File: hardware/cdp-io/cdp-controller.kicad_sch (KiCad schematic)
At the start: 10 parts, among them U10 74LS175, U7 74LS14, U8 74LS138, U9 74LS138

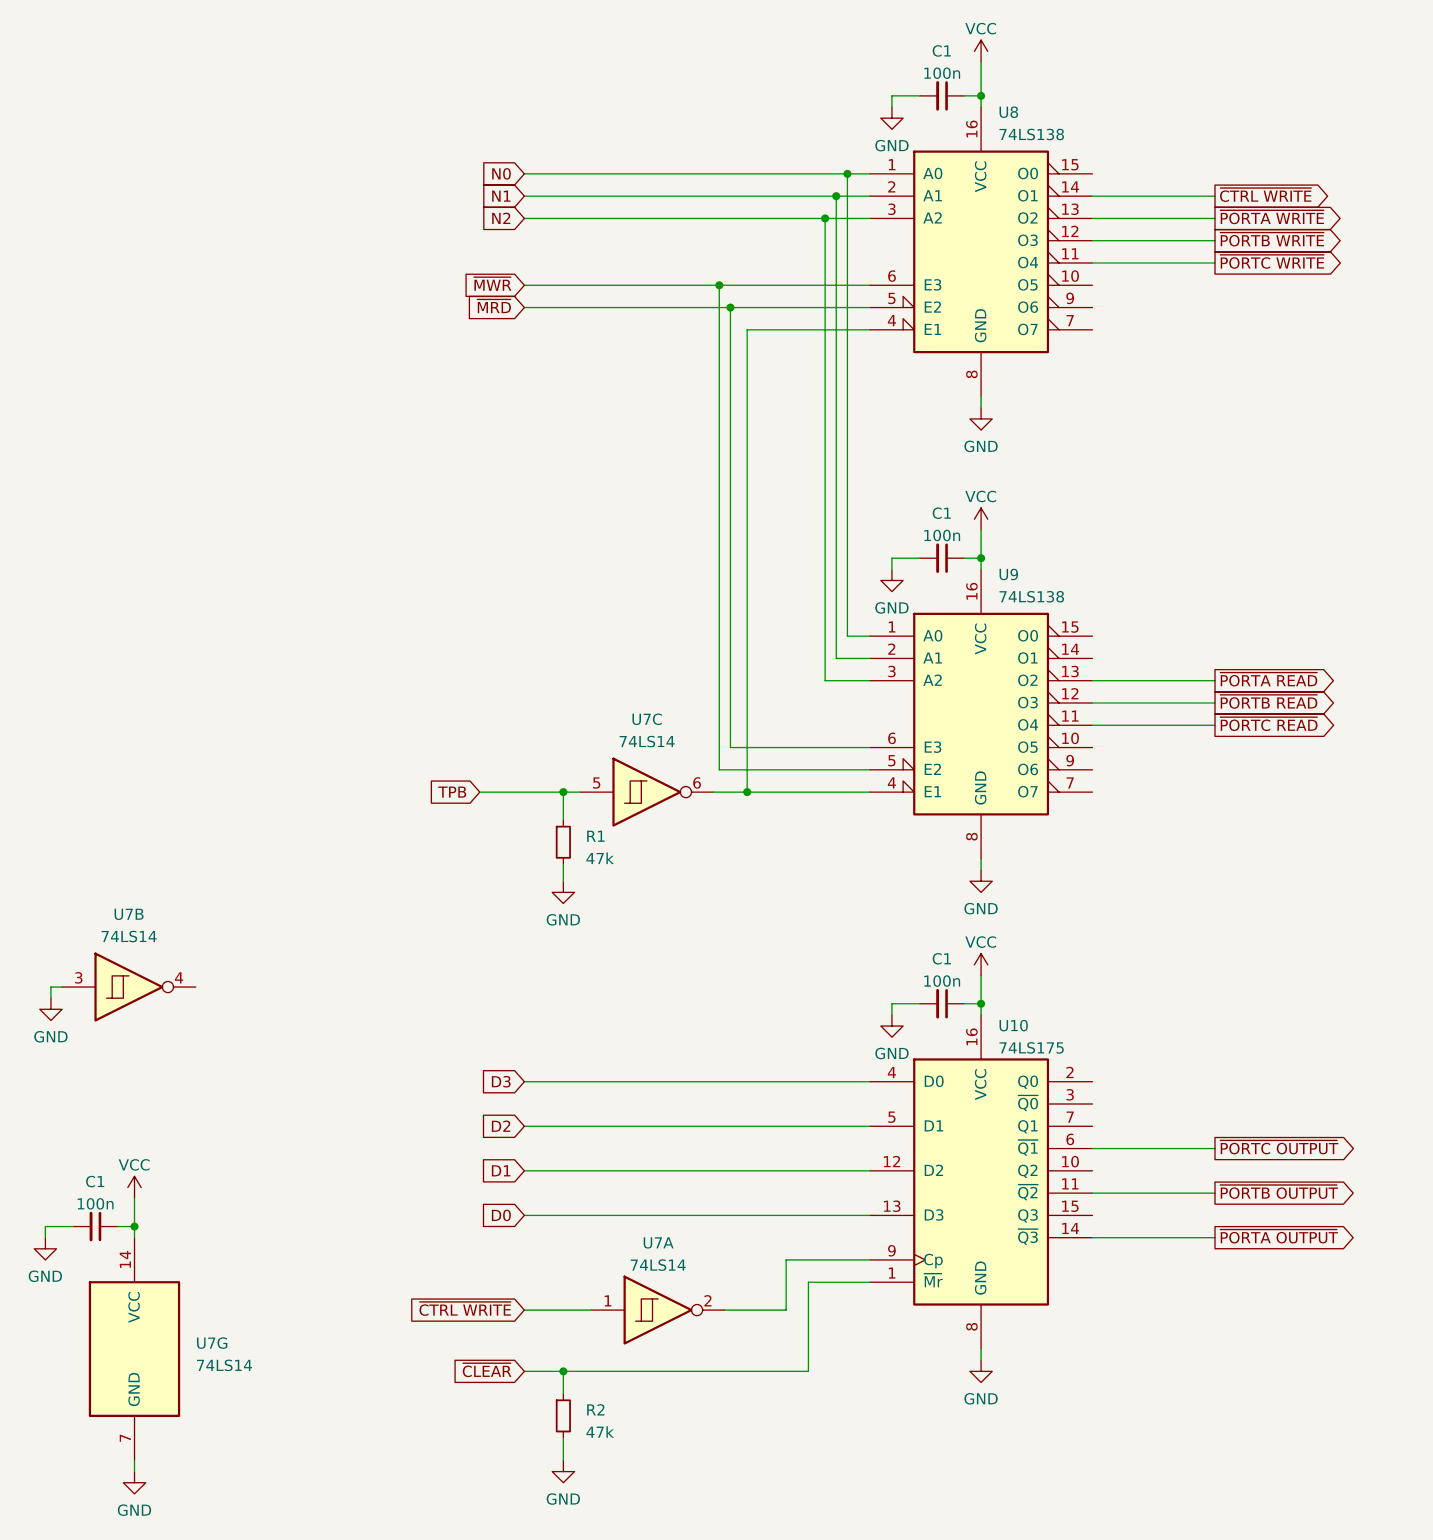
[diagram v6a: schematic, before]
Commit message: IC names fixed. PCB is updated. Gerber files are still ok.
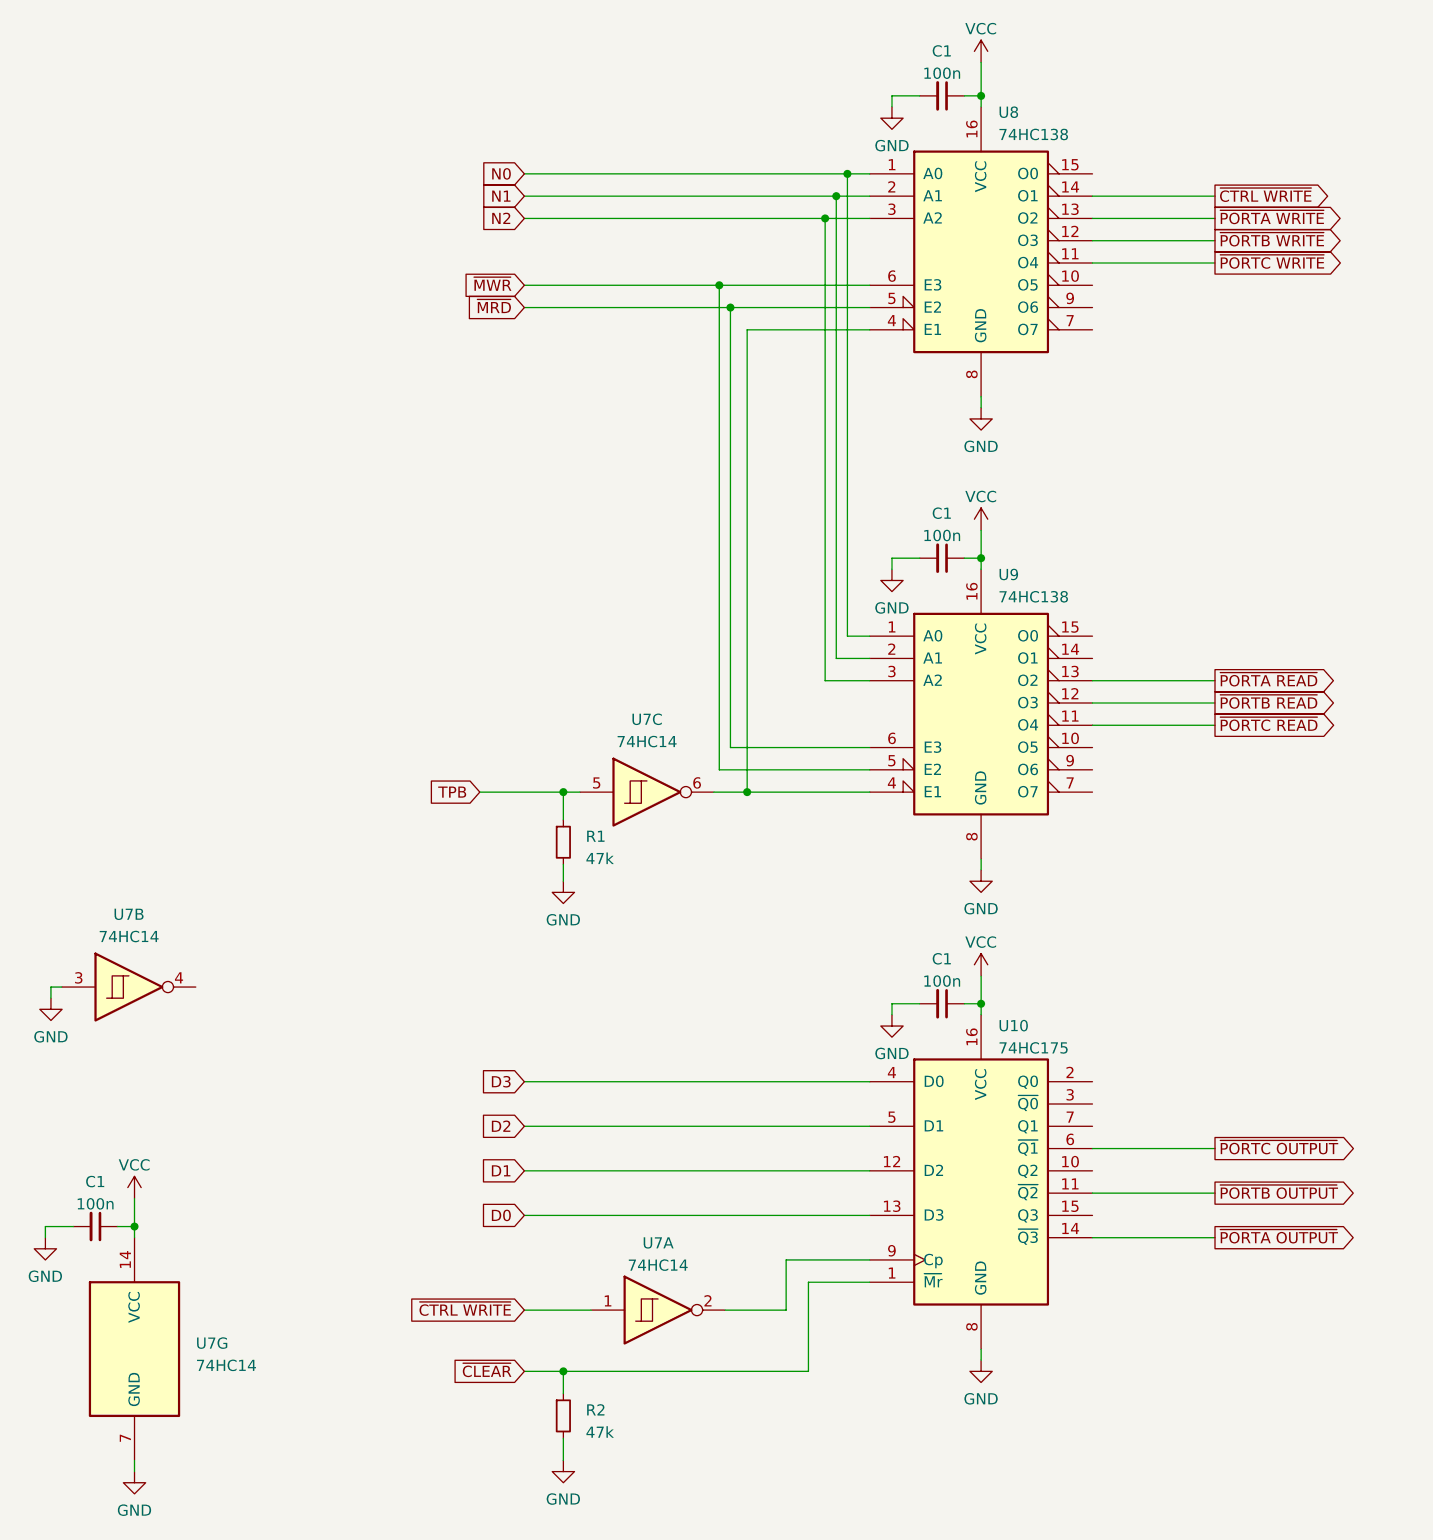
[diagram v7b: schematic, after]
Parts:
- U10: value 74LS175 -> 74HC175
- U7: value 74LS14 -> 74HC14
- U8, U9: value 74LS138 -> 74HC138
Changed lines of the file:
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@@
       (effects (font (size 1.27 1.27)) (justify left))
     )
-    (property "Value" "74LS138" (at 144.8309 30.48 0)
+    (property "Value" "74HC138" (at 144.8309 30.48 0)
       (effects (font (size 1.27 1.27)) (justify left))
     )
@@
       (effects (font (size 1.27 1.27)) (justify left))
     )
-    (property "Value" "74LS138" (at 144.8309 83.185 0)
+    (property "Value" "74HC138" (at 144.8309 83.185 0)
       (effects (font (size 1.27 1.27)) (justify left))
     )
@@
       (effects (font (size 1.27 1.27)))
     )
-    (property "Value" "74LS14" (at 106.045 159.385 0)
+    (property "Value" "74HC14" (at 106.045 159.385 0)
       (effects (font (size 1.27 1.27)))
     )
@@
       (effects (font (size 1.27 1.27)))
     )
-    (property "Value" "74LS14" (at 45.72 121.92 0)
+    (property "Value" "74HC14" (at 45.72 121.92 0)
       (effects (font (size 1.27 1.27)))
     )
@@
       (effects (font (size 1.27 1.27)) (justify left))
     )
-    (property "Value" "74LS14" (at 53.34 170.815 0)
+    (property "Value" "74HC14" (at 53.34 170.815 0)
       (effects (font (size 1.27 1.27)) (justify left))
     )
@@
       (effects (font (size 1.27 1.27)))
     )
-    (property "Value" "74LS14" (at 104.775 99.695 0)
+    (property "Value" "74HC14" (at 104.775 99.695 0)
       (effects (font (size 1.27 1.27)))
     )
@@
       (effects (font (size 1.27 1.27)) (justify left))
     )
-    (property "Value" "74LS175" (at 144.8309 134.62 0)
-      (effects (font (size 1.27 1.27)) (justify left))
-    )
+    (property "Value" "74HC175" (at 144.8309 134.62 0)
+      (effects (font (size 1.27 1.27)) (justify left))
+    )
